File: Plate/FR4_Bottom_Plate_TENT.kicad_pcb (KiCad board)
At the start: 2 copper layers, 145.7 x 107.7 mm, 10 parts

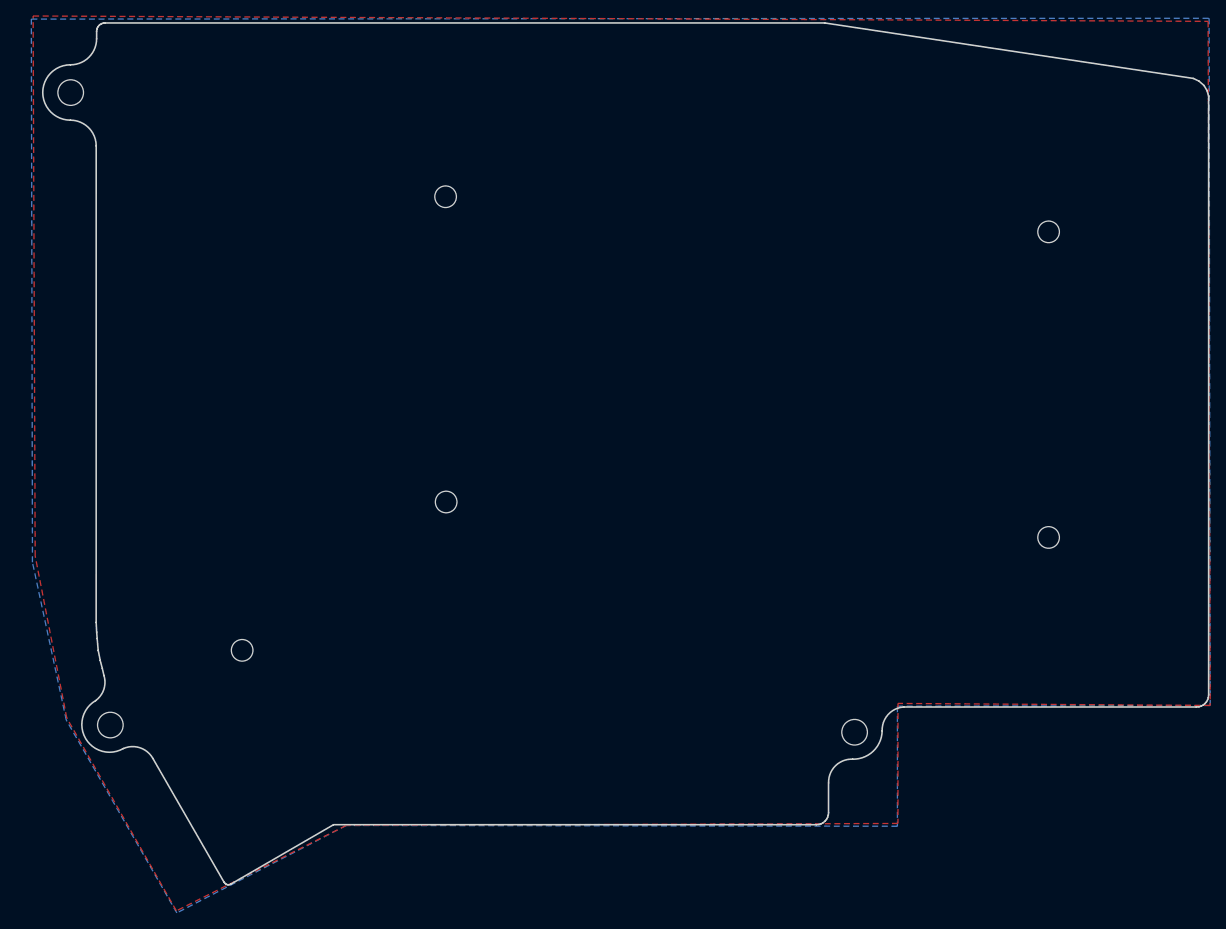
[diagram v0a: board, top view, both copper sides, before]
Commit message: Updated plates
Plates now have no copper layer, both preparing for wireless, and to avoid scratches/shorting, if OLED etc. is not soldered with flat pads.
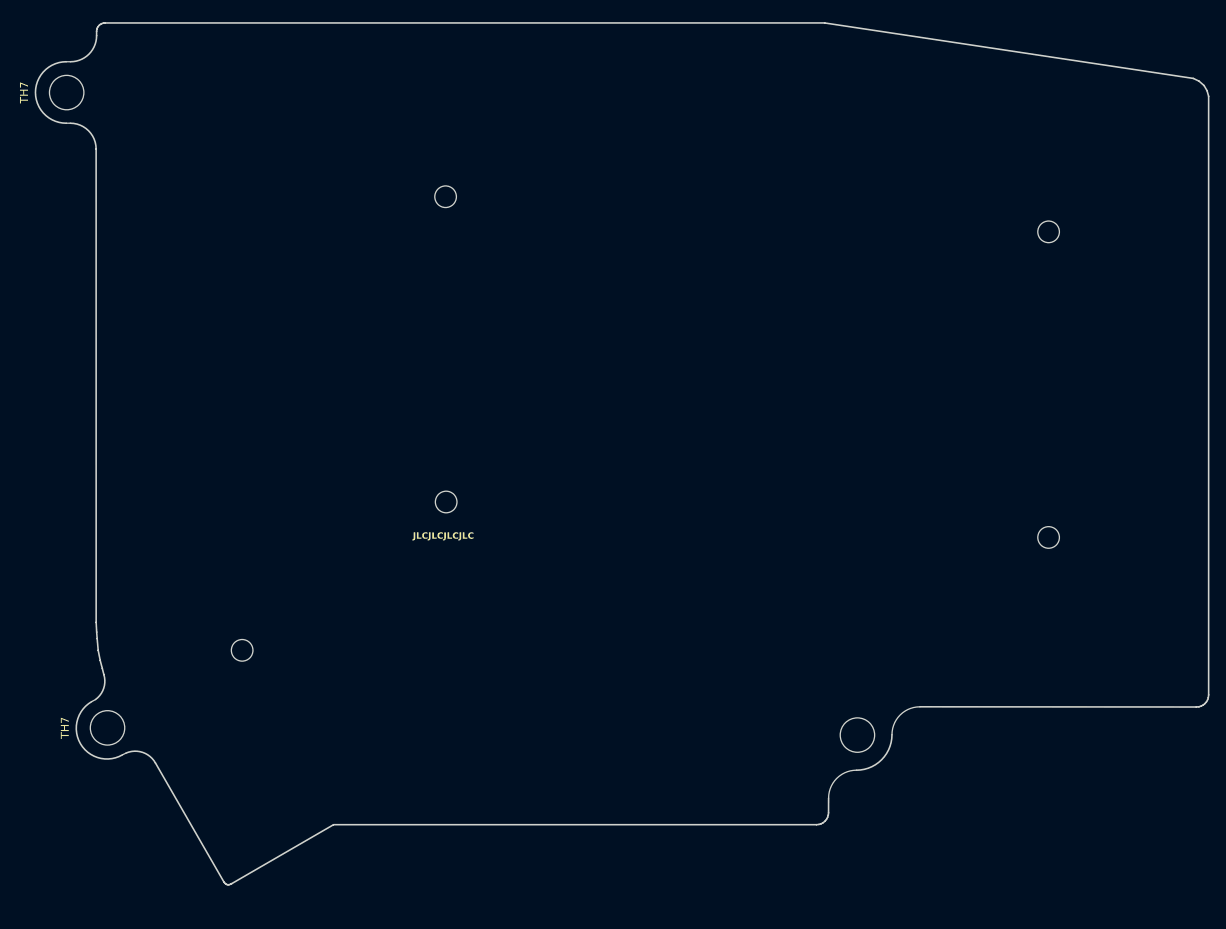
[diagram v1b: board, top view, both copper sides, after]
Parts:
- TH7 (x3): footprint MountingHole:MountingHole_3.2mm_M3 -> MountingHole:MountingHole_4.3mm_M4
- moved TH7 0.50 mm to (77.0, 44.4)
- moved TH7 0.50 mm to (175.8, 124.7)
- moved TH7 0.50 mm to (82.1, 123.8)
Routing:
- removed copper zone on B.Cu, net (none)
- removed copper zone on F.Cu, net (none)
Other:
- board size 145.7 x 107.7 mm -> 146.6 x 107.7 mm
- board text added: "JLCJLCJLCJLC"

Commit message: Revert "Merge pull request #53 from TweetyDaBird/release"
This reverts commit d5395b9879702c31b6de7b44cd45c4487da02165, reversing
changes made to 721366541e1b3daa08e8a27e832954bcb38f5212.

# Conflicts:
#	.gitignore
#	Lotus 58 Classic/v1.26/Lotus58_Glow_126.kicad_pcb
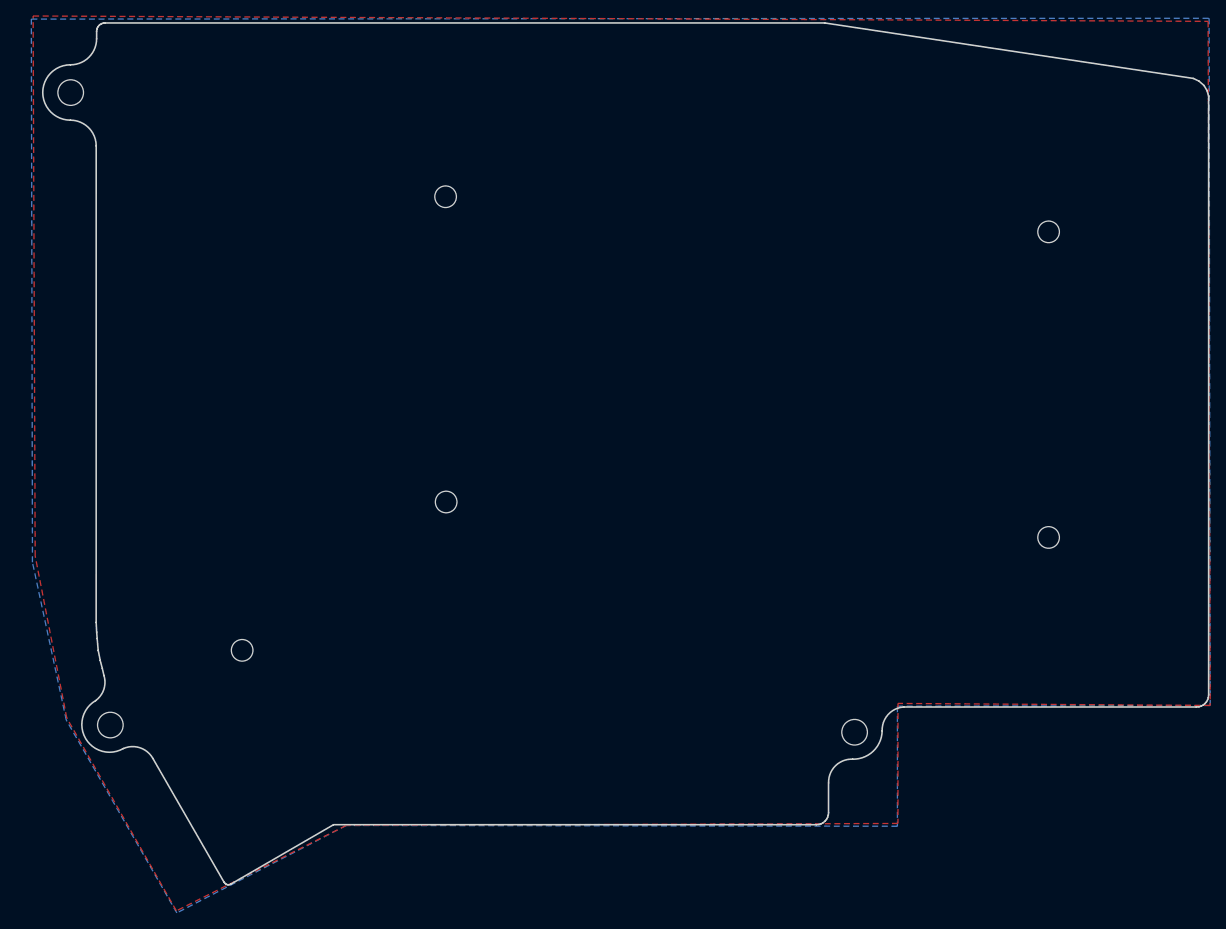
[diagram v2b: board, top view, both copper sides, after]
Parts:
- TH7 (x3): footprint MountingHole:MountingHole_4.3mm_M4 -> MountingHole:MountingHole_3.2mm_M3
- moved TH7 0.50 mm to (77.5, 44.4)
- moved TH7 0.50 mm to (175.4, 124.3)
- moved TH7 0.50 mm to (82.4, 123.5)
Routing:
- added copper zone on B.Cu, net (none)
- added copper zone on F.Cu, net (none)
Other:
- board size 146.6 x 107.7 mm -> 145.7 x 107.7 mm
- board text removed: "JLCJLCJLCJLC"
